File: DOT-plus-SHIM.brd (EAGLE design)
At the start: 56 x 65 mm, 3 parts

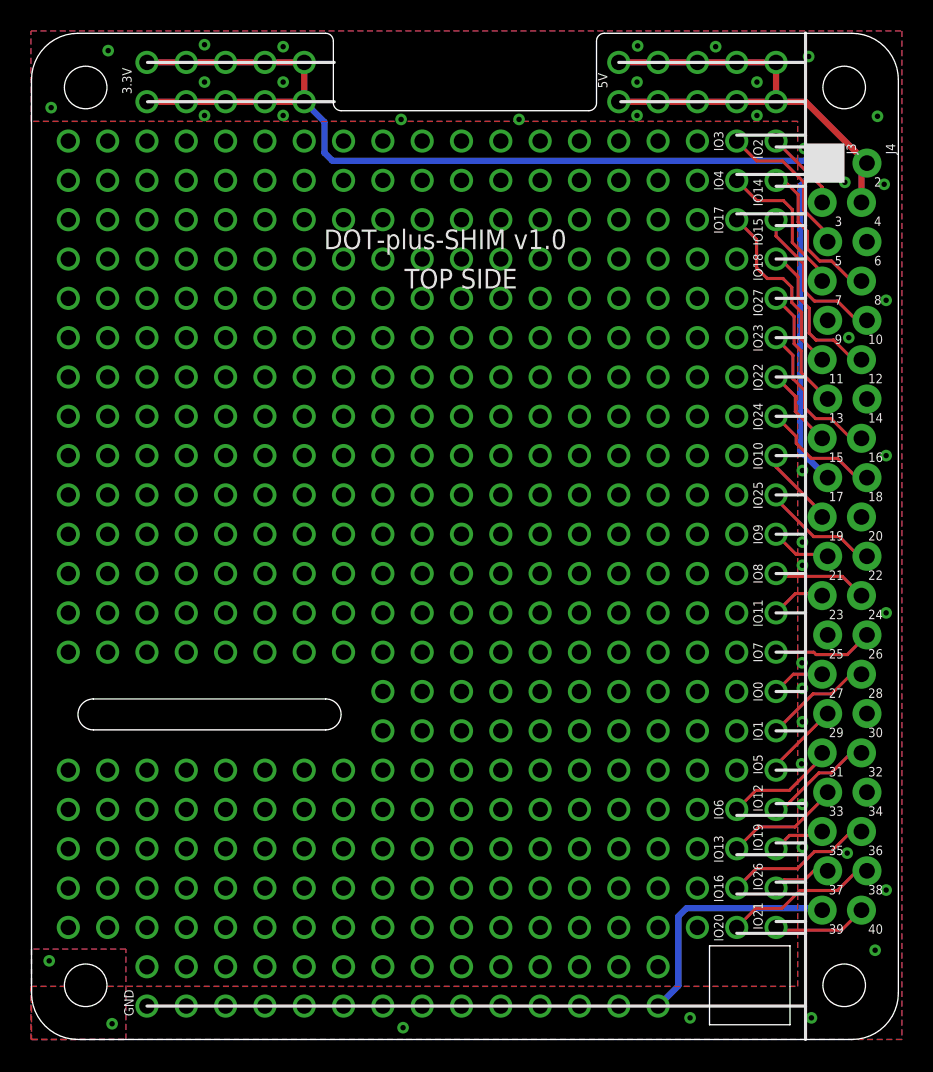
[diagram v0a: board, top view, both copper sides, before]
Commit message: Reworked A+/B+ board corners
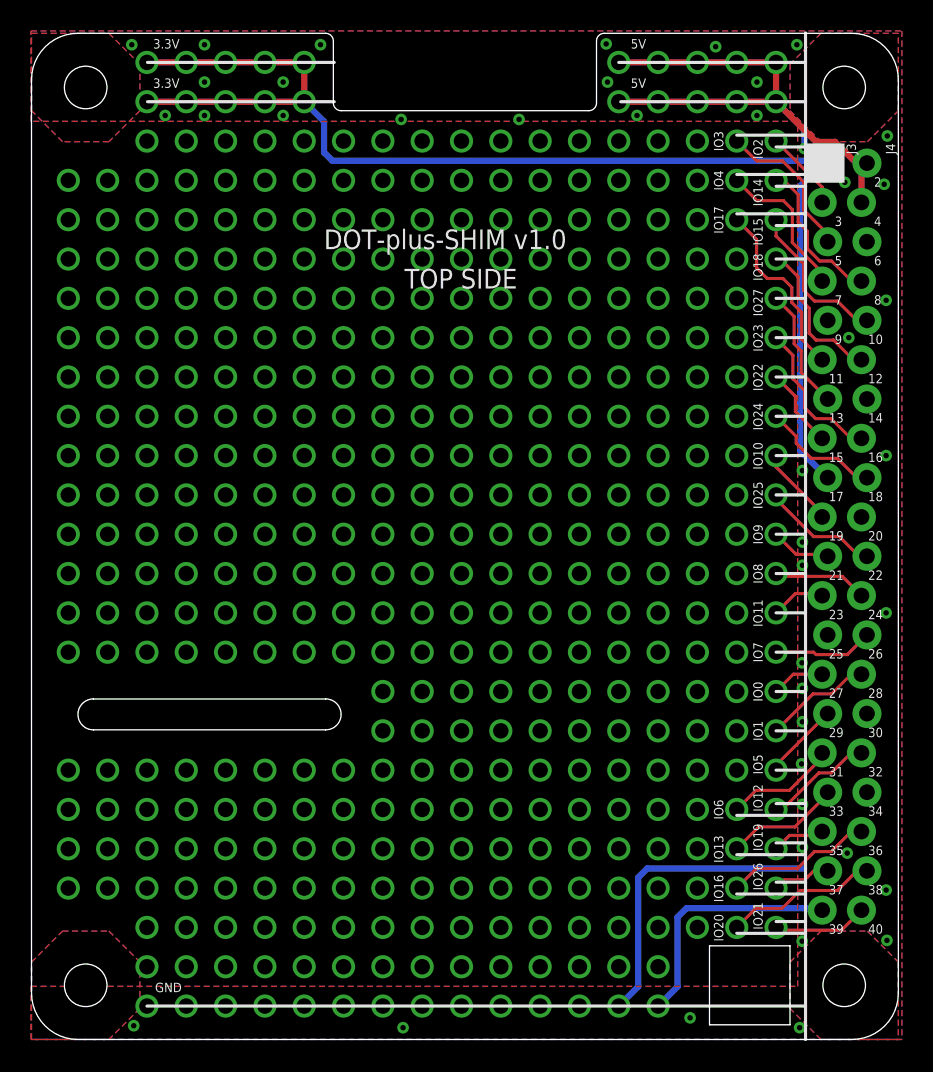
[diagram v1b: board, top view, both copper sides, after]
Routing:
- net GND: track 15.9 -> 37.9 mm
- added copper zone on layer 1, net GND1
- added copper zone on layer 16, net GND1
